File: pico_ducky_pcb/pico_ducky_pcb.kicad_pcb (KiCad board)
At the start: 4 copper layers, 14 x 30 mm, 31 parts, among them J1 USB_A, J2 Conn_01x03_Female, SW1 R-667799, SW2 R-667799, U1 AP2138N-3.3, U2 W25Q32JVZP, U3 RP2040, Y1 Crystal_GND24

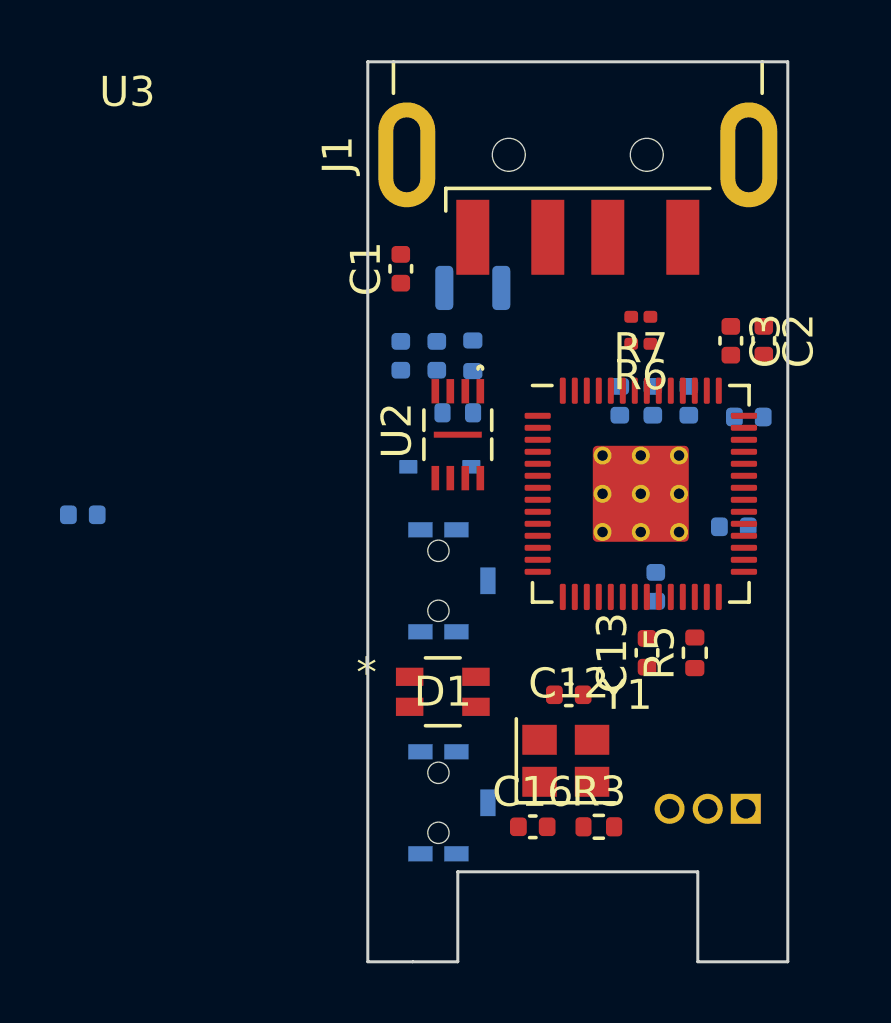
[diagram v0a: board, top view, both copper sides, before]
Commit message: finish most of the inpours, routing and vias
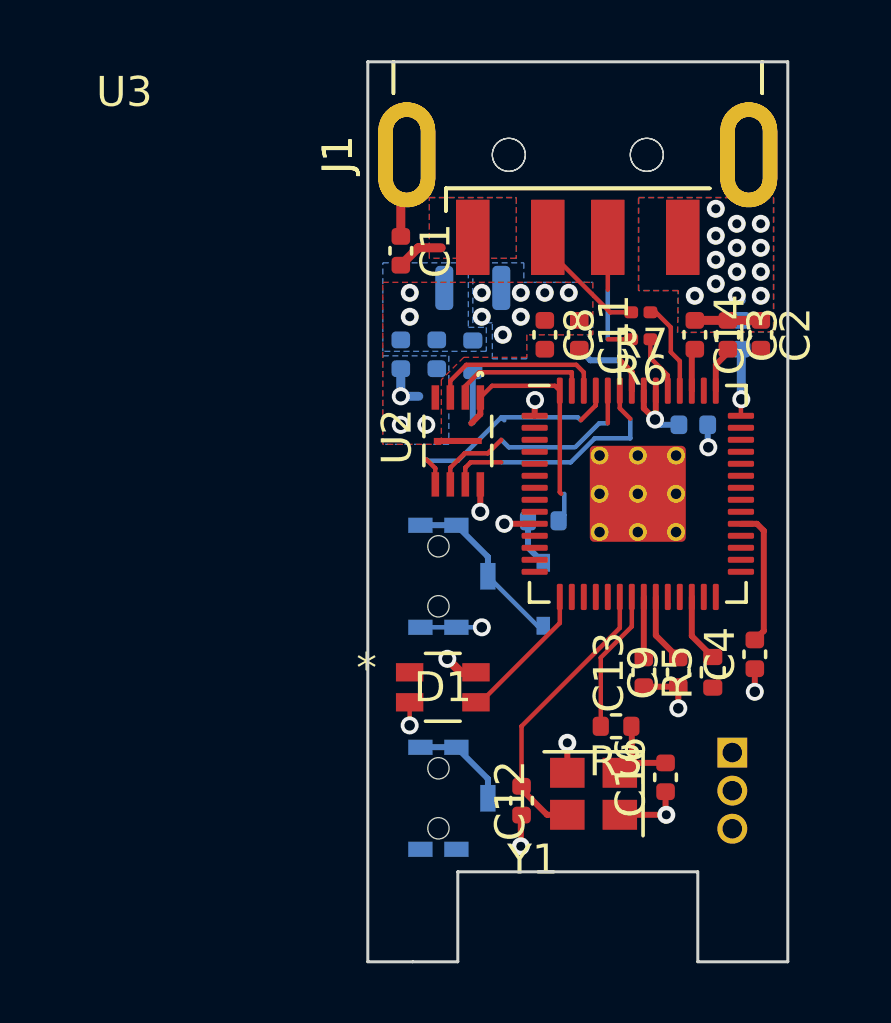
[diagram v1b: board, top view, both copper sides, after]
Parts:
- added J1: USB_A, Connector_USB:USB_A_CNCTech_1001-011-01101_Horizontal, F.Cu at (87.0, 36.2)
- C11, C14, C4, C8, C9: moved to F.Cu
- moved C6 20.6 mm to (90.8, 52.1)
- moved D2 5.47 mm to (85.8, 57.8), turned to 90 degrees
- moved C16 4.72 mm to (89.9, 63.9), turned to 90 degrees
- moved R4 4.59 mm to (85.8, 55.3)
- moved C4 4.31 mm to (92.9, 59.8), turned to 90 degrees
- moved C8 4.22 mm to (85.9, 49.1), turned to -90 degrees
- moved C12 3.87 mm to (85.1, 64.6), turned to 90 degrees
- moved R3 3.40 mm to (88.3, 62.1), turned to 180 degrees
- moved C9 2.95 mm to (90.3, 60.4), turned to 90 degrees
- moved C7 2.75 mm to (92.5, 49.1), turned to -90 degrees
- moved C11 2.58 mm to (87.0, 49.1), turned to -90 degrees
- moved C14 2.21 mm to (90.9, 49.1), turned to -90 degrees
- moved J2 1.93 mm to (92.2, 63.0), turned to 180 degrees
- moved Y1 1.44 mm to (87.5, 64.4), turned to 180 degrees
- moved R5 0.88 mm to (91.5, 60.4)
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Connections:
- D1 pad 4: +5V -> +3V3
- U2 pad 6: /QSPI_CLK -> /QSPI_SCLK
- U3 pad 15: unconnected-(U3-Pad15) -> /RGB_DI
- U3 pad 27: /RGB_DI -> unconnected-(U3-Pad27)
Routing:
- net GND: track 0.00 -> 17.7 mm, vias 0 -> 33
- net +3V3: track 0.00 -> 17.0 mm, vias 0 -> 6
- net /QSPI_CS: track 0.00 -> 10.1 mm
- net /X_IN: track 0.00 -> 9.68 mm
- net /QSPI_SD3: track 0.00 -> 8.19 mm
- net /QSPI_SD0: track 0.00 -> 8.11 mm
- net /QSPI_SCLK: track 0.00 -> 7.68 mm
- net +1V1: track 0.00 -> 6.45 mm
- net /QSPI_SD2: track 0.00 -> 5.94 mm
- net /USB_BOOT: track 0.00 -> 5.87 mm
- net /RESET: track 0.00 -> 5.63 mm
- net /USB_-: track 0.00 -> 4.76 mm
- net /RGB_DI: track 0.00 -> 4.76 mm
- net /X_OUT: track 0.00 -> 4.74 mm
- net /QSPI_SD1: track 0.00 -> 4.73 mm
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- added copper zone on B.Cu, net +3V3
- added copper zone on In2.Cu, net +3V3
- added copper zone on B.Cu, net +5V
- added copper zone on F.Cu, net +5V
- added copper zone on B.Cu, net GND
- added copper zone on F.Cu, net GND
- added copper zone on In1.Cu, net GND
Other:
- board text added: "Layout on 0.1mm"

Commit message: git ignore
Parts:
- moved R5 0.68 mm to (91.9, 59.8)
- moved C4 0.11 mm to (93.0, 59.8)
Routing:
- net +1V1: track 6.45 -> 17.3 mm
- net /SWCLK: track 0.00 -> 9.14 mm
- net /SWD: track 0.00 -> 7.51 mm
- net /QSPI_SD3: track 8.19 -> 5.87 mm
- net GND: track 17.7 -> 19.9 mm
- net +3V3: track 17.0 -> 18.5 mm, vias 6 -> 9
- net /RESET: track 5.63 -> 6.58 mm, vias 0 -> 1
- net /USB_BOOT: track 5.87 -> 6.81 mm, vias 0 -> 1

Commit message: pass erc
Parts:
- added C5: 0.1uF, Capacitor_SMD:C_0201_0603Metric, F.Cu at (81.1, 53.8)
- C10, C11, C13, C15, C3, C4, C7, C8, C9: footprint Capacitor_SMD:C_0402_1005Metric -> Capacitor_SMD:C_0201_0603Metric
- D1: value WS2812C -> SK6812; footprint WS2812C:WS2812C-2020 -> LED_SMD:LED_SK6812_EC15_1.5x1.5mm
- R6, R7: footprint Resistor_SMD:R_0201_0603Metric -> Resistor_SMD:R_0402_1005Metric
- U1: value AP2138N-3.3 -> AP2127K-3.3; footprint Package_TO_SOT_SMD:SOT-23 -> Package_TO_SOT_SMD:SOT-23-5
- moved U1 1.30 mm to (83.0, 47.8), turned to 0 degrees
- moved C10 1.05 mm to (82.3, 50.8)
- moved C15 1.05 mm to (81.1, 50.8)
- moved R2 0.80 mm to (83.5, 50.6)
- turned D1 to 90 degrees
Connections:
- D1 pad 1: unconnected-(D1-Pad1) -> GND
- D1 pad 2: GND -> /RGB_DI
- D1 pad 3: /RGB_DI -> +3V3
- D1 pad 4: +3V3 -> unconnected-(D1-Pad4)
- U1 pad 1: GND -> +5V
- U1 pad 2: +3V3 -> GND
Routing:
- net /RESET: track 6.58 -> 17.0 mm
- net GND: track 19.9 -> 26.8 mm, vias 33 -> 16
- net /USB_BOOT: track 6.81 -> 13.7 mm
- net /QSPI_CS: track 10.1 -> 7.32 mm
- net +3V3: track 18.5 -> 21.2 mm
- net +5V: track 1.59 -> 0.00 mm, vias 0 -> 2
- net /QSPI_SD3: track 5.87 -> 7.26 mm, vias 0 -> 1
- net /RGB_DI: track 4.76 -> 5.39 mm
- net /QSPI_SCLK: track 7.68 -> 7.13 mm, vias 0 -> 2
- net /QSPI_SD0: track 8.11 -> 7.89 mm, vias 0 -> 2
- net (no net): vias 0 -> 3

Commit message: finish the layout
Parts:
- removed the J1 at (87.0, 36.2)
- C10, C15, C7: moved to F.Cu
- moved C14 2.56 mm to (93.5, 48.9)
- moved C2 2.41 mm to (90.7, 48.9)
- moved C10 0.91 mm to (82.2, 49.9), turned to 180 degrees
- moved C15 0.60 mm to (81.1, 51.4)
- moved C9 0.37 mm to (90.0, 60.3)
- moved C11 0.35 mm to (86.7, 49.1)
- moved C3 0.35 mm to (91.7, 49.1)
- moved R7 0.15 mm to (89.1, 48.2)
- moved C13 0.05 mm to (89.2, 60.3)
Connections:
- C14 pad 2: +1V1 -> +3V3
- C2 pad 2: +3V3 -> +1V1
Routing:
- net GND: track 26.8 -> 31.0 mm, vias 16 -> 15
- net +3V3: track 21.2 -> 22.5 mm, vias 9 -> 11
- net /QSPI_CS: track 7.32 -> 8.21 mm, vias 0 -> 2
- net /QSPI_SD3: track 7.26 -> 8.12 mm, vias 1 -> 2
- net /USB_-: track 4.76 -> 4.05 mm
- net +1V1: track 17.3 -> 17.7 mm, vias 0 -> 1
- net /USB_+: track 4.18 -> 4.23 mm, vias 0 -> 2
- net +5V: vias 2 -> 3
- net (no net): vias 3 -> 0
- added copper zone on F.Cu, net +3V3
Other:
- board text added: "Layout on 0.1mm Traces on 0.01mm"
- board text added: "RST"
- board text added: "USB Boot"
- board text removed: "Layout on 0.1mm"

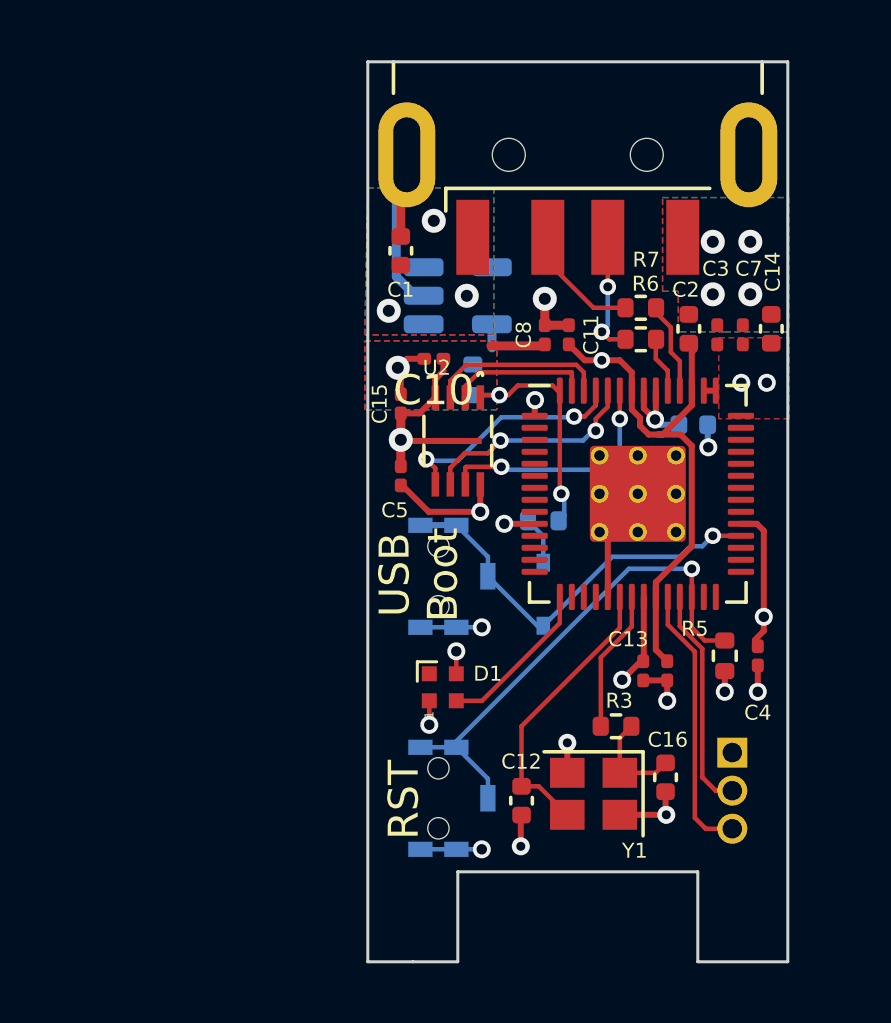
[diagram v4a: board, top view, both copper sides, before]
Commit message: fix silk screen adnd use 10 pin JTAG programmer
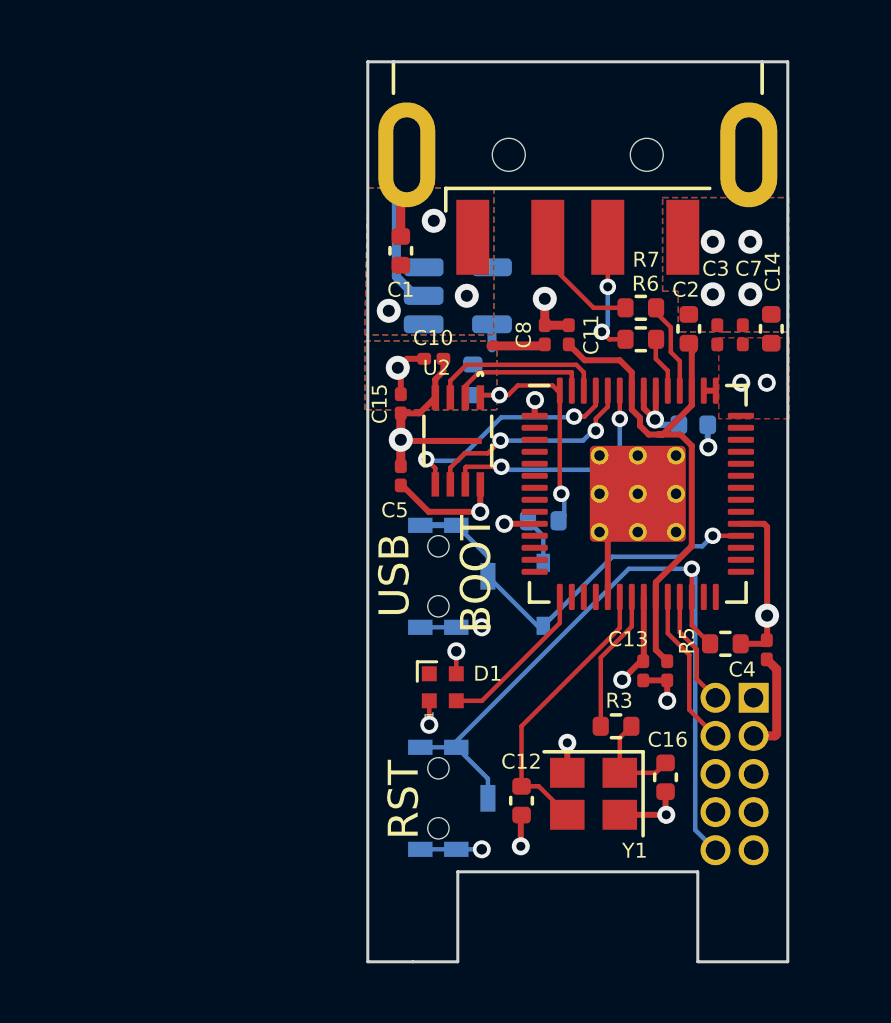
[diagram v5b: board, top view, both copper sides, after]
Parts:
- removed J2: Conn_01x03_Female, Connector_PinHeader_1.27mm:PinHeader_1x03_P1.27mm_Vertical
- added J3: Conn_ARM_JTAG_SWD_10, Connector_PinHeader_1.27mm:PinHeader_2x05_P1.27mm_Vertical, B.Cu at (92.9, 61.2)
- moved R5 0.40 mm to (91.9, 59.4), turned to 180 degrees
- moved C4 0.36 mm to (93.3, 59.6)
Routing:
- net /RESET: track 17.0 -> 26.2 mm
- net /SWCLK: track 9.14 -> 5.29 mm
- net /SWD: track 7.51 -> 3.86 mm
- net GND: track 31.0 -> 32.6 mm, vias 15 -> 14
- net /USB_-: track 4.05 -> 3.22 mm
- net +3V3: track 22.5 -> 22.6 mm, vias 11 -> 10
- net +1V1: vias 1 -> 0
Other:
- board text added: "BOOT"
- board text added: "RP Duck V1"
- board text added: "USB"
- board text removed: "USB Boot"

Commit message: just leave the project behind in the v1 folder
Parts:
- removed C3: 0.1uF, Capacitor_SMD:C_0201_0603Metric
- C5, C8: footprint Capacitor_SMD:C_0201_0603Metric -> Capacitor_SMD:C_0402_1005Metric; moved to B.Cu
- R2: moved to F.Cu
- U2: footprint 8-UFDFN:W25Q80DVUXIE TR -> Package_SON:USON-8_3x4mm_P0.4mm
- moved C10 7.02 mm to (84.3, 56.6), turned to 90 degrees
- moved C15 5.41 mm to (85.6, 48.5), turned to -90 degrees
- moved C8 5.35 mm to (90.9, 51.0), turned to 180 degrees
- moved C11 4.96 mm to (91.7, 49.1)
- moved C5 4.75 mm to (85.8, 53.6), turned to 180 degrees
- moved R2 3.68 mm to (86.6, 48.7)
- moved SW1 0.75 mm to (82.1, 57.9)
- moved U2 0.55 mm to (82.5, 52.7)
- moved D1 0.40 mm to (82.3, 61.2)
- moved C6 0.05 mm to (90.9, 52.1)
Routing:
- net /QSPI_CS: track 7.95 -> 10.2 mm, vias 2 -> 3
- net +1V1: track 17.7 -> 15.5 mm
- net /QSPI_SCLK: track 7.42 -> 9.07 mm
- net /QSPI_SD0: track 7.83 -> 8.85 mm
- net GND: track 32.6 -> 33.3 mm
- net /QSPI_SD3: track 8.12 -> 8.80 mm
- net +3V3: track 22.6 -> 22.3 mm, vias 10 -> 11
- net +5V: vias 3 -> 2
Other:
- outline, holes or cut-outs redrawn
- board text removed: "BOOT"
